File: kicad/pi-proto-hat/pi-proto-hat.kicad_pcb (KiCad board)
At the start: 2 copper layers, 65 x 56 mm, 10 parts, among them J1 Conn_01x22_Male, J2 Conn_02x22_Top_Bottom, P1 Conn_02x20_Odd_Even

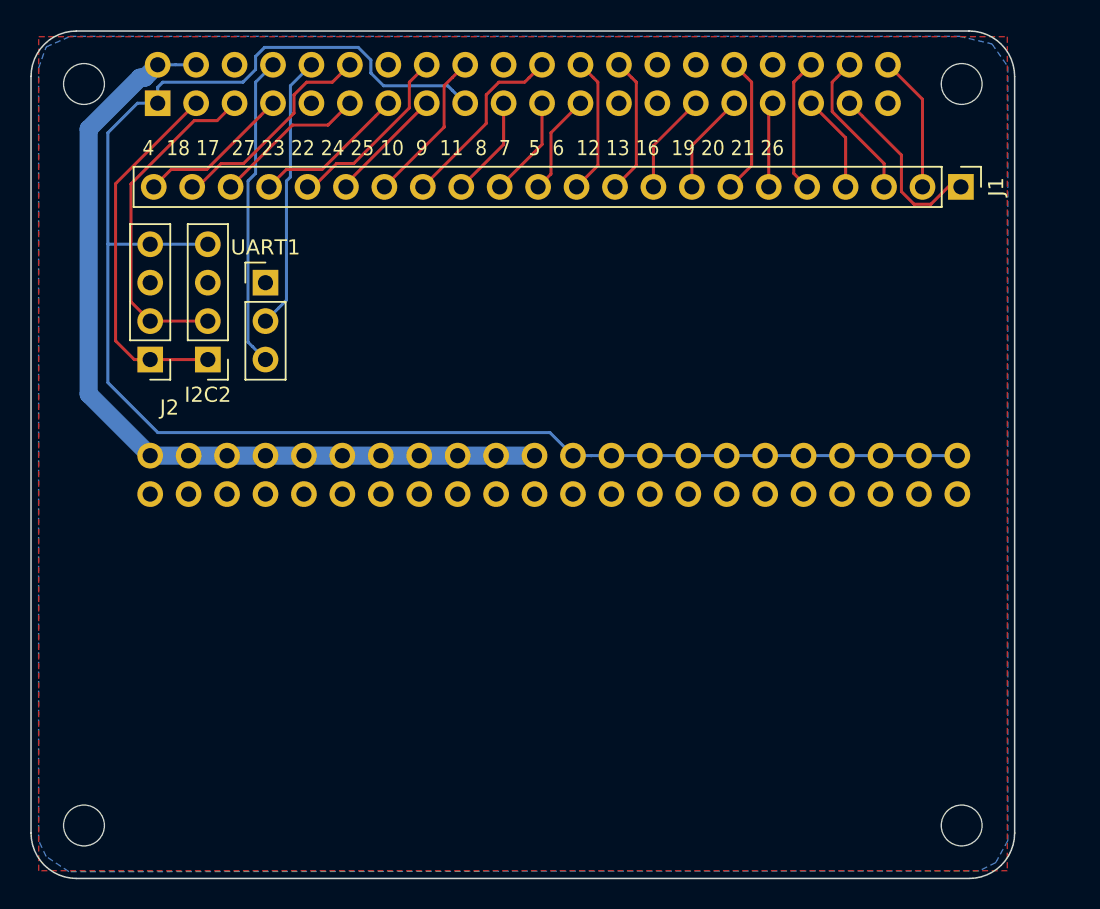
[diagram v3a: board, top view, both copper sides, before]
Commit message: changed footprints, added two prototype-areas
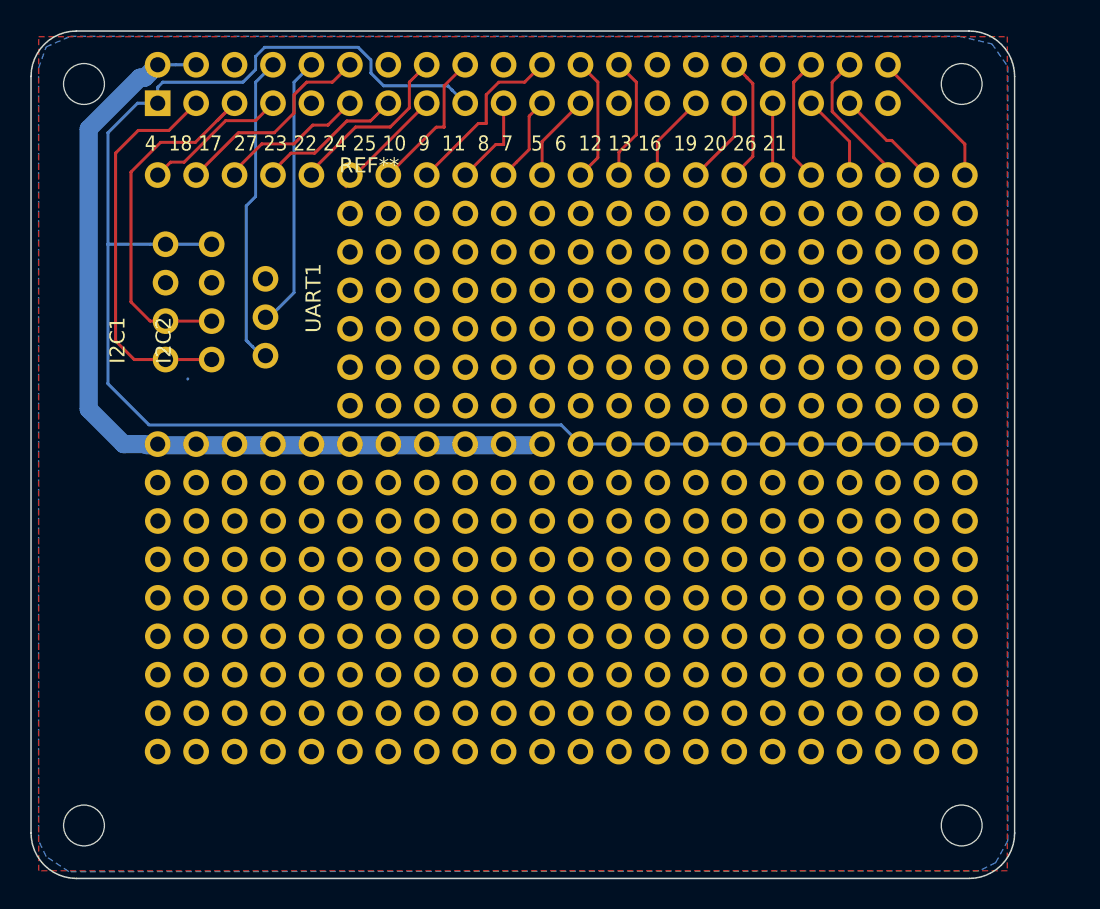
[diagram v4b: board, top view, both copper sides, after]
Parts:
- added J3: Conn_01x22_Male, Proto_Area:Proto_Area_22x01, F.Cu at (261.7, 141.6)
- added REF**: Proto_Area_22x06_P2.54mm_Drill1.0mm, Proto_Area:Proto_Area_22x06, F.Cu at (208.4, 126.4)
- added REF**: Proto_Area_17x06_P2.54mm_Drill1.0mm, Proto_Area:Proto_Area_17x06, F.Cu at (221.1, 106.1)
- I2C1, I2C2: footprint Connector_PinHeader_2.54mm:PinHeader_1x04_P2.54mm_Vertical -> Proto_Area:Proto_Area_04x01
- J1: footprint Connector_PinHeader_2.54mm:PinHeader_1x22_P2.54mm_Vertical -> Proto_Area:Proto_Area_22x01
- UART1: footprint Connector_PinHeader_2.54mm:PinHeader_1x03_P2.54mm_Vertical -> Proto_Area:Proto_Area_03x01
- moved I2C1 1.02 mm to (208.9, 115.7), turned to 90 degrees
- moved J2 0.91 mm to (208.4, 121.3)
- moved J1 0.82 mm to (261.7, 103.5), turned to 180 degrees
- moved I2C2 0.25 mm to (211.9, 115.7), turned to 90 degrees
- moved UART1 0.25 mm to (215.5, 110.4), turned to 270 degrees
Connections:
- J1 pad 1: /GPIO26 -> /GPIO21(SPI1_SCK)
- J1 pad 2: /GPIO21(SPI1_SCK) -> /GPIO26
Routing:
- net /GPIO26: track 12.0 -> 7.12 mm
- net /GPIO3(SCL1): track 22.5 -> 24.5 mm
- net /GPIO20(SPI1_MOSI): track 9.97 -> 8.42 mm
- net /GPIO2(SDA1): track 24.5 -> 25.7 mm
- net /GPIO6: track 6.69 -> 5.80 mm
- net /GPIO11(SPI0_SCK): track 6.69 -> 5.80 mm
- net /GPIO8(SPI0_CE_0): track 9.13 -> 8.24 mm
- net /GPIO7(SPI1_CE_1): track 9.13 -> 8.24 mm
- net /GPIO9(SPI0_MISO): track 6.69 -> 5.80 mm
- net /GPIO5: track 6.69 -> 5.80 mm
- net /GPIO12(PWM0): track 9.13 -> 8.31 mm
- net /GPIO19(SPI1_MISO): track 6.47 -> 5.80 mm
- net /GPIO16: track 8.91 -> 8.24 mm
- net /GPIO25(GEN6): track 12.3 -> 11.7 mm
- net /GPIO24(GEN5): track 10.3 -> 9.70 mm
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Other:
- board text added: "4 18 17 27 23 22 24 25 10 9 11 8 7 5 6 12 13 16 19 20 26 21"
- board text removed: "4 18 17 27 23 22 24 25 10 9 11 8 7 5 6 12 13 16 19 20 21 26"
- board text removed: "RASPBERRY-PI 40-PIN ADDON BOARD VIEW FROM TOP NOTE: P1 SHOULD BE FITTED ON THE REVERSE OF THE BOARD ADD EDGE CUTS FROM CAMERA AND DISPLAY PORTS AS REQUIRED"

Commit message: added routing for second GPIO connector
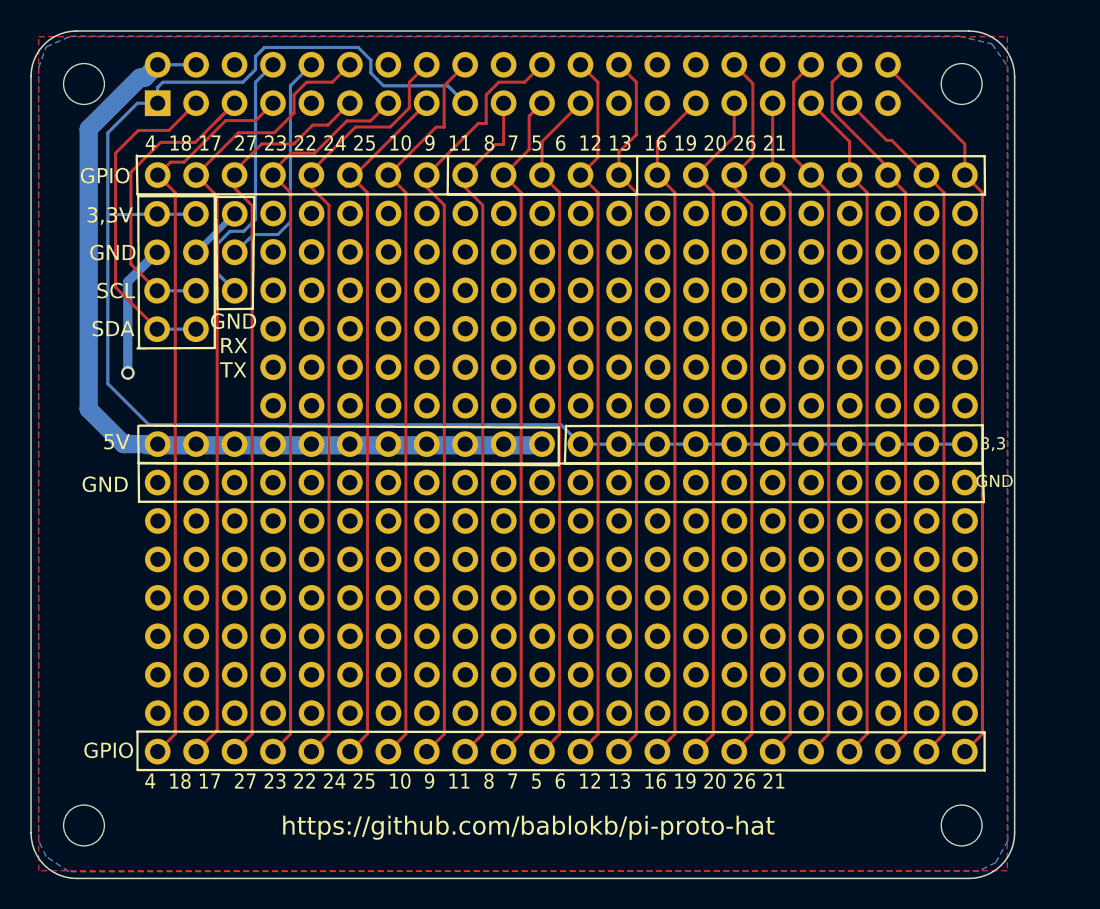
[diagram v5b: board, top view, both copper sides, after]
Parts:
- removed the REF** at (221.1, 106.1)
- added REF**: Proto_Area_17x06_P2.54mm_Drill1.0mm, Proto_Area:Proto_Area_19x06, F.Cu at (216.0, 106.1)
- moved UART1 4.75 mm to (213.5, 106.1)
- moved I2C2 2.26 mm to (210.9, 113.7)
- moved I2C1 2.08 mm to (208.3, 113.7)
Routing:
- net /GPIO18(GEN1)(PWM0): track 13.9 -> 53.1 mm
- net /GPIO21(SPI1_SCK): track 9.39 -> 48.5 mm
- net /GPIO20(SPI1_MOSI): track 8.42 -> 47.5 mm
- net /GPIO8(SPI0_CE_0): track 8.24 -> 47.3 mm
- net /GPIO7(SPI1_CE_1): track 8.24 -> 47.3 mm
- net /GPIO6: track 5.80 -> 44.9 mm
- net /GPIO5: track 5.80 -> 44.9 mm
- net /GPIO4(GCLK): track 9.59 -> 48.6 mm
- net /GPIO27(GEN2): track 9.85 -> 48.9 mm
- net /GPIO25(GEN6): track 11.7 -> 50.8 mm
- net /GPIO23(GEN4): track 11.9 -> 51.0 mm
- net /GPIO19(SPI1_MISO): track 5.80 -> 44.9 mm
- net /GPIO17(GEN0): track 9.85 -> 48.9 mm
- net /GPIO13(PWM1): track 5.12 -> 44.2 mm
- net /GPIO11(SPI0_SCK): track 5.80 -> 44.9 mm
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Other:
- board text added: "3,3"
- board text added: "3,3V"
- board text added: "5V"
- board text added: "GND"
- board text added: "GND RX TX"
- board text added: "GPIO"
- board text added: "SCL"
- board text added: "SDA"
- board text added: "https://github.com/bablokb/pi-proto-hat"

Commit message: changed/added prototyping areas to fill pcb
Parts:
- added REF**: Proto_Area_03x02_P2.54mm_Drill1.0mm, Proto_Area:Proto_Area_03x02, F.Cu at (208.4, 116.2)
- REF**: footprint Proto_Area:Proto_Area_22x06 -> Proto_Area:Proto_Area_24x06
- moved REF** 5.08 mm to (203.3, 126.4)
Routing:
- net /GPIO14(TXD0): track 17.5 -> 20.0 mm
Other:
- board text added: "RX"
- board text added: "TX"
- board text removed: "GND RX TX"

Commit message: removed unnecessary trace / configured gerber-plot
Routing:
- net /GPIO14(TXD0): track 20.0 -> 17.5 mm
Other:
- board text added: "JLCJLCJLCJLC"
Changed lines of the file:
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@@
   (general
     (thickness 1.6)
-    (drawings 70)
-    (tracks 248)
+    (drawings 71)
+    (tracks 246)
     (zones 0)
     (modules 14)
@@
     (visible_elements 7FFFFFFF)
     (pcbplotparams
-      (layerselection 0x00030_80000001)
-      (usegerberextensions true)
-      (usegerberattributes false)
+      (layerselection 0x010f0_ffffffff)
+      (usegerberextensions false)
+      (usegerberattributes true)
       (usegerberadvancedattributes false)
       (creategerberjobfile false)
@@
       (viasonmask false)
       (mode 1)
-      (useauxorigin false)
+      (useauxorigin true)
       (hpglpennumber 1)
       (hpglpenspeed 20)
@@
       (outputformat 1)
       (mirror false)
-      (drillshape 1)
+      (drillshape 0)
       (scaleselection 1)
-      (outputdirectory ""))
+      (outputdirectory "/home/bablokb/git/pi-proto-hat/kicad/pi-proto-hat/plot/"))
   )
   (net 0 "")
@@
     (pad 1 np_thru_hole circle (at 0 0 180) (size 2.7 2.7) (drill 2.7) (layers *.Cu *.Mask))
   )
+  (gr_text JLCJLCJLCJLC (at 253.0606 147.968) (layer F.SilkS)
+    (effects (font (size 1 1) (thickness 0.15)))
+  )
   (gr_text RX (at 213.4112 109.9442) (layer F.SilkS)
     (effects (font (size 1 1) (thickness 0.15)))
@@
     (effects (font (size 1 1) (thickness 0.15)))
   )
-  (gr_text https://github.com/bablokb/pi-proto-hat (at 232.8422 146.5456) (layer F.SilkS)
+  (gr_text https://github.com/bablokb/pi-proto-hat (at 226.67 146.1392) (layer F.SilkS)
     (effects (font (size 1.2 1.2) (thickness 0.18)))
   )
@@
   (segment (start 214.064801 107.233401) (end 213.149997 107.233401) (width 0.2) (layer B.Cu) (net 10))
   (segment (start 214.839999 106.458203) (end 214.064801 107.233401) (width 0.2) (layer B.Cu) (net 10))
-  (segment (start 213.462 113.6272) (end 213.4366 113.6526) (width 0.2) (layer F.Cu) (net 10))
-  (segment (start 213.462 111.1634) (end 213.462 113.6272) (width 0.2) (layer F.Cu) (net 10))
   (segment (start 214.337399 107.798801) (end 213.4874 108.6488) (width 0.2) (layer B.Cu) (net 11))
   (segment (start 214.688201 107.447999) (end 214.337399 107.798801) (width 0.2) (layer B.Cu) (net 11))
